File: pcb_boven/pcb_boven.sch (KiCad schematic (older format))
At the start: 28 parts

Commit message: pcb onder gemaakt
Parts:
- added BZ1: Buzzer, symbol Device:Buzzer
- added U1: miniIMU-9_v6, custom:miniIMU-9_v6, symbol miniimu-9_v6:miniIMU-9_v6
- gave numbers to parts that had none: 1
- renumbered control_board to control_board1, dip_swith_instellinen to dip_swith_instellinen1, goal_kleur to goal_kleur1
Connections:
- net labels added: A, B
- wire segments 204 -> 234
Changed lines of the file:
@@
 $EndDescr
 $Comp
-L openmv_m7_r2:openMV_M7_R2 U?
+L openmv_m7_r2:openMV_M7_R2 U2
 U 1 1 66360711
 P 9350 5325
-F 0 "U?" H 9350 6490 50  0000 C CNN
+F 0 "U2" H 9350 6490 50  0000 C CNN
 F 1 "openMV_M7_R2" H 9350 6399 50  0000 C CNN
 F 2 "custom:openmv_m7_r2" H 9350 6675 50  0001 C CNN
@@
 $EndComp
 $Comp
-L teensy:Teensy4.1 control_board
+L teensy:Teensy4.1 control_board1
 U 1 1 66362D60
 P 6125 8750
-F 0 "control_board" H 6125 11315 50  0000 C CNN
+F 0 "control_board1" H 6125 11315 50  0000 C CNN
 F 1 "Teensy4.1" H 6125 11224 50  0000 C CNN
 F 2 "" H 5725 9150 50  0001 C CNN
@@
 $EndComp
 $Comp
-L Switch:SW_DIP_x06 dip_swith_instellinen
+L Switch:SW_DIP_x06 dip_swith_instellinen1
 U 1 1 66364D70
 P 3575 7200
-F 0 "dip_swith_instellinen" H 3575 7767 50  0000 C CNN
+F 0 "dip_swith_instellinen1" H 3575 7767 50  0000 C CNN
 F 1 "SW_DIP_x06" H 3575 7676 50  0000 C CNN
 F 2 "" H 3575 7200 50  0001 C CNN
@@
 $EndComp
 $Comp
-L Switch:SW_DIP_x01 goal_kleur
+L Switch:SW_DIP_x01 goal_kleur1
 U 1 1 66365885
 P 10775 5125
-F 0 "goal_kleur" H 10775 4858 50  0000 C CNN
+F 0 "goal_kleur1" H 10775 4858 50  0000 C CNN
 F 1 "SW_DIP_x01" H 10775 4949 50  0000 C CNN
 F 2 "" H 10775 5125 50  0001 C CNN
@@
 $EndComp
 Wire Wire Line
-	7225 7300 8100 7300
+	7225 7300 7350 7300
 Wire Wire Line
 	8100 7300 8100 10775
@@
 scl
 Wire Wire Line
-	7225 7400 8075 7400
+	7225 7400 7425 7400
 Wire Wire Line
 	8075 7400 8075 10675
@@
 gnd
 Wire Wire Line
-	7225 6600 8150 6600
+	7225 6600 7675 6600
 Wire Wire Line
 	8150 6600 8150 10975
@@
 Connection ~ 4200 6025
 Wire Wire Line
-	4800 6025 7550 6025
+	4800 6025 7275 6025
 Wire Wire Line
 	7550 6025 7550 6700
@@
 	10025 4450 10025 5825
 Connection ~ 10025 5825
+$Comp
+L Device:Buzzer BZ1
+U 1 1 663737AA
+P 3950 8225
+F 0 "BZ1" H 3955 8515 50  0000 C CNN
+F 1 "Buzzer" H 3955 8424 50  0000 C CNN
+F 2 "" V 3925 8325 50  0001 C CNN
+F 3 "~" V 3925 8325 50  0001 C CNN
+	1    3950 8225
+	-1   0    0    -1
+$EndComp
+Wire Wire Line
+	4050 8125 4500 8125
+Wire Wire Line
+	4500 8125 4500 7500
+Wire Wire Line
+	4500 7500 5025 7500
+Wire Wire Line
+	2900 6025 4050 6025
+Wire Wire Line
+	4050 8325 4300 8325
+Connection ~ 4050 6025
+Wire Wire Line
+	2900 8475 4300 8475
+Wire Wire Line
+	4300 8475 4300 8325
+Wire Wire Line
+	2900 6025 2900 8475
+$Comp
+L miniimu-9_v6:miniIMU-9_v6 U1
+U 1 1 663B967A
+P 7050 4650
+F 0 "U1" H 7528 4538 50  0000 L CNN
+F 1 "miniIMU-9_v6" H 7528 4447 50  0000 L CNN
+F 2 "custom:miniIMU-9_v6" H 7050 5100 50  0001 C CNN
+F 3 "" H 7050 5100 50  0001 C CNN
+	1    7050 4650
+	1    0    0    -1
+$EndComp
+Wire Wire Line
+	7150 5250 7150 5550
+Wire Wire Line
+	7150 5550 7275 5550
+Wire Wire Line
+	7275 5550 7275 6025
+Connection ~ 7275 6025
+Wire Wire Line
+	7275 6025 7550 6025
+Wire Wire Line
+	7675 6600 7675 5500
+Wire Wire Line
+	7675 5500 7250 5500
+Wire Wire Line
+	7250 5500 7250 5250
+Connection ~ 7675 6600
+Wire Wire Line
+	7675 6600 8150 6600
+Wire Wire Line
+	7050 5250 7050 6175
+Wire Wire Line
+	7050 6175 7425 6175
+Wire Wire Line
+	7425 6175 7425 7400
+Connection ~ 7425 7400
+Wire Wire Line
+	7425 7400 8075 7400
+Wire Wire Line
+	7350 7300 7350 6250
+Wire Wire Line
+	7350 6250 6950 6250
+Wire Wire Line
+	6950 6250 6950 5250
+Connection ~ 7350 7300
+Wire Wire Line
+	7350 7300 8100 7300
+Text GLabel 1300 10175 0    50   Input ~ 0
+A
+Text GLabel 1300 10075 0    50   Input ~ 0
+B
+Wire Wire Line
+	4800 7700 5025 7700
+Wire Wire Line
+	950  10175 4800 10175
+Wire Wire Line
+	4800 10175 4800 7700
+Wire Wire Line
+	5025 7600 4775 7600
+Wire Wire Line
+	4775 7600 4775 10075
+Wire Wire Line
+	4775 10075 950  10075
 $EndSCHEMATC

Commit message: pcb onder gemaakt
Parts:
- BZ1: footprint (none) -> custom:buzer
- control_board1: footprint (none) -> custom:teensy4.1
- dip_swith_instellinen1: footprint (none) -> custom:dipswitch6
- goal_kleur1: footprint (none) -> custom:dipswitch1
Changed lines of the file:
@@
 F 0 "control_board1" H 6125 11315 50  0000 C CNN
 F 1 "Teensy4.1" H 6125 11224 50  0000 C CNN
-F 2 "" H 5725 9150 50  0001 C CNN
+F 2 "custom:teensy4.1" H 5725 9150 50  0001 C CNN
 F 3 "" H 5725 9150 50  0001 C CNN
 	1    6125 8750
@@
 F 0 "dip_swith_instellinen1" H 3575 7767 50  0000 C CNN
 F 1 "SW_DIP_x06" H 3575 7676 50  0000 C CNN
-F 2 "" H 3575 7200 50  0001 C CNN
+F 2 "custom:dipswitch6" H 3575 7200 50  0001 C CNN
 F 3 "~" H 3575 7200 50  0001 C CNN
 	1    3575 7200
@@
 F 0 "goal_kleur1" H 10775 4858 50  0000 C CNN
 F 1 "SW_DIP_x01" H 10775 4949 50  0000 C CNN
-F 2 "" H 10775 5125 50  0001 C CNN
+F 2 "custom:dipswitch1" H 10775 5125 50  0001 C CNN
 F 3 "~" H 10775 5125 50  0001 C CNN
 	1    10775 5125
@@
 F 0 "BZ1" H 3955 8515 50  0000 C CNN
 F 1 "Buzzer" H 3955 8424 50  0000 C CNN
-F 2 "" V 3925 8325 50  0001 C CNN
+F 2 "custom:buzer" V 3925 8325 50  0001 C CNN
 F 3 "~" V 3925 8325 50  0001 C CNN
 	1    3950 8225

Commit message: pcb onder gemaakt
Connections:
- wire segments 234 -> 238
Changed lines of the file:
@@
 	10025 5825 10025 6975
-Wire Wire Line
-	10025 6975 9100 6975
-Wire Wire Line
-	9100 6975 9100 10375
-Wire Wire Line
-	9100 10375 950  10375
 Wire Wire Line
 	9075 10275 9075 6800
@@
 Text GLabel 1300 10275 0    50   Input ~ 0
 3.3v
-Text GLabel 1300 10375 0    50   Input ~ 0
-gnd
 Wire Wire Line
 	11025 6800 9075 6800
@@
 Wire Wire Line
 	4775 10075 950  10075
+Wire Wire Line
+	8125 6700 8350 6700
+Wire Wire Line
+	8625 6700 8625 6975
+Wire Wire Line
+	8625 6975 10025 6975
+Connection ~ 8125 6700
+Wire Wire Line
+	8350 2350 8350 6700
+Connection ~ 8350 2350
+Connection ~ 8350 6700
+Wire Wire Line
+	8350 6700 8625 6700
+Wire Wire Line
+	8200 2375 8200 5825
+Wire Wire Line
+	8200 5825 8700 5825
+Connection ~ 8200 2375
+Connection ~ 8700 5825
 $EndSCHEMATC

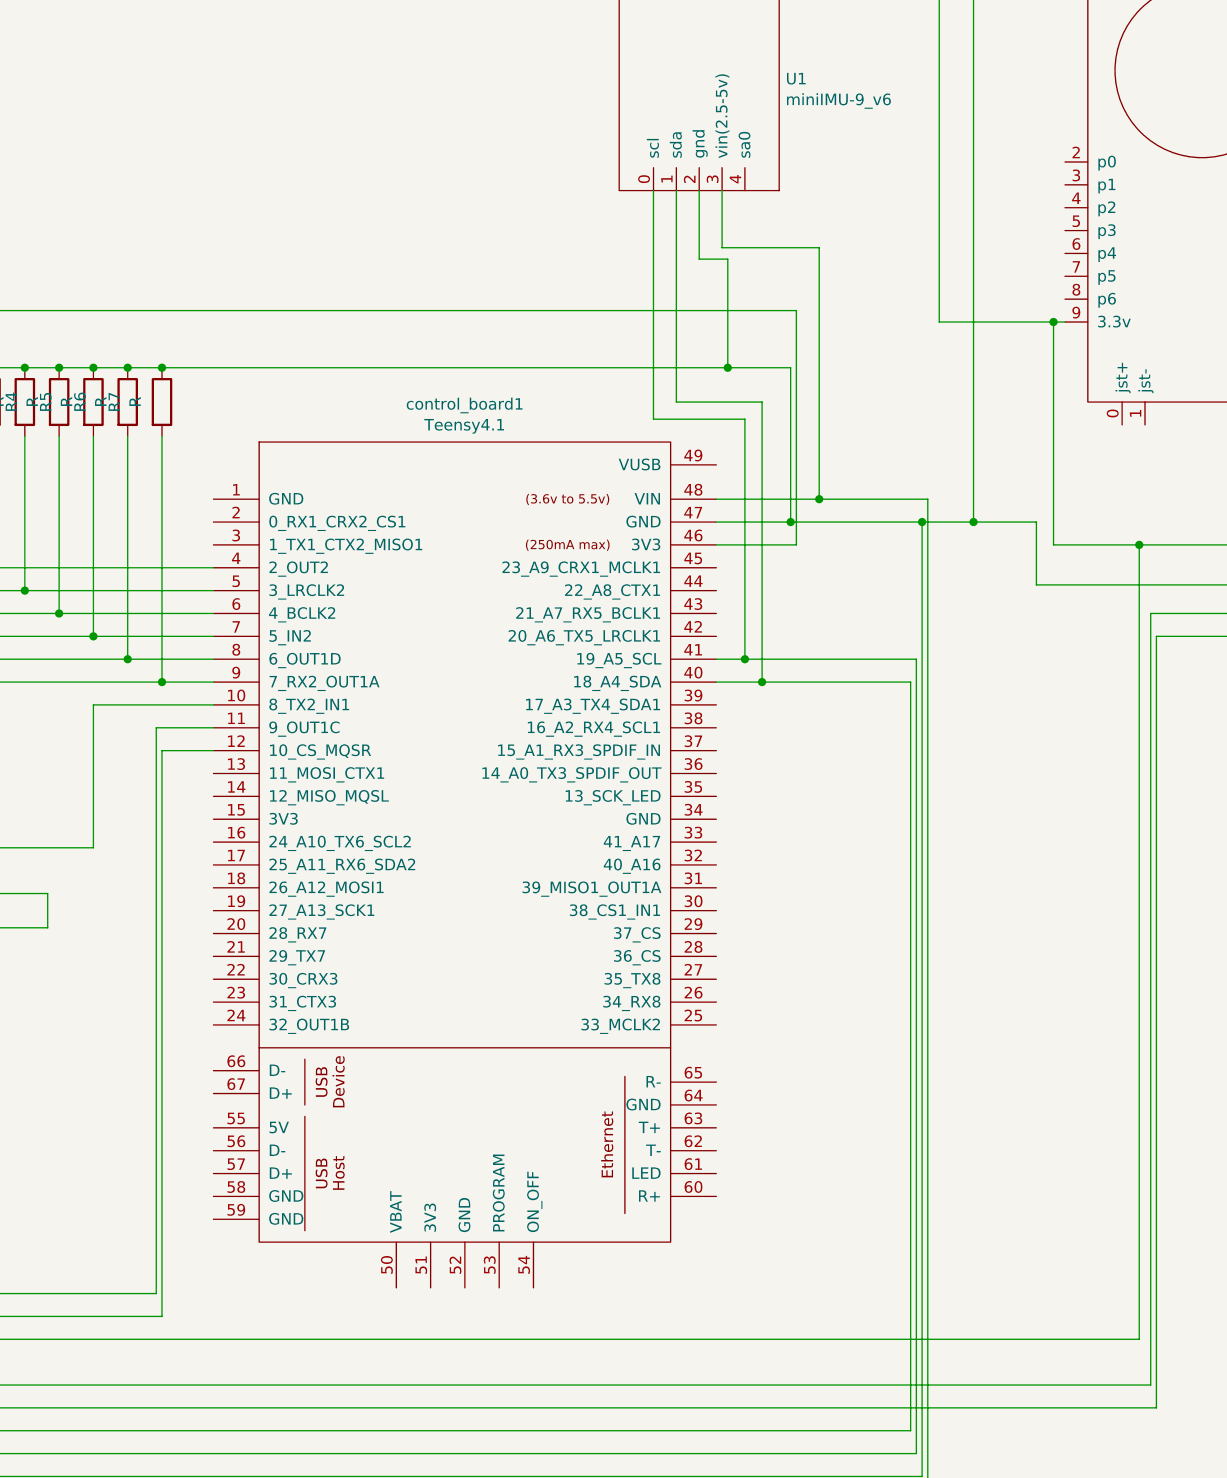
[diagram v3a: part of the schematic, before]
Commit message: add connect between teensy and openmv
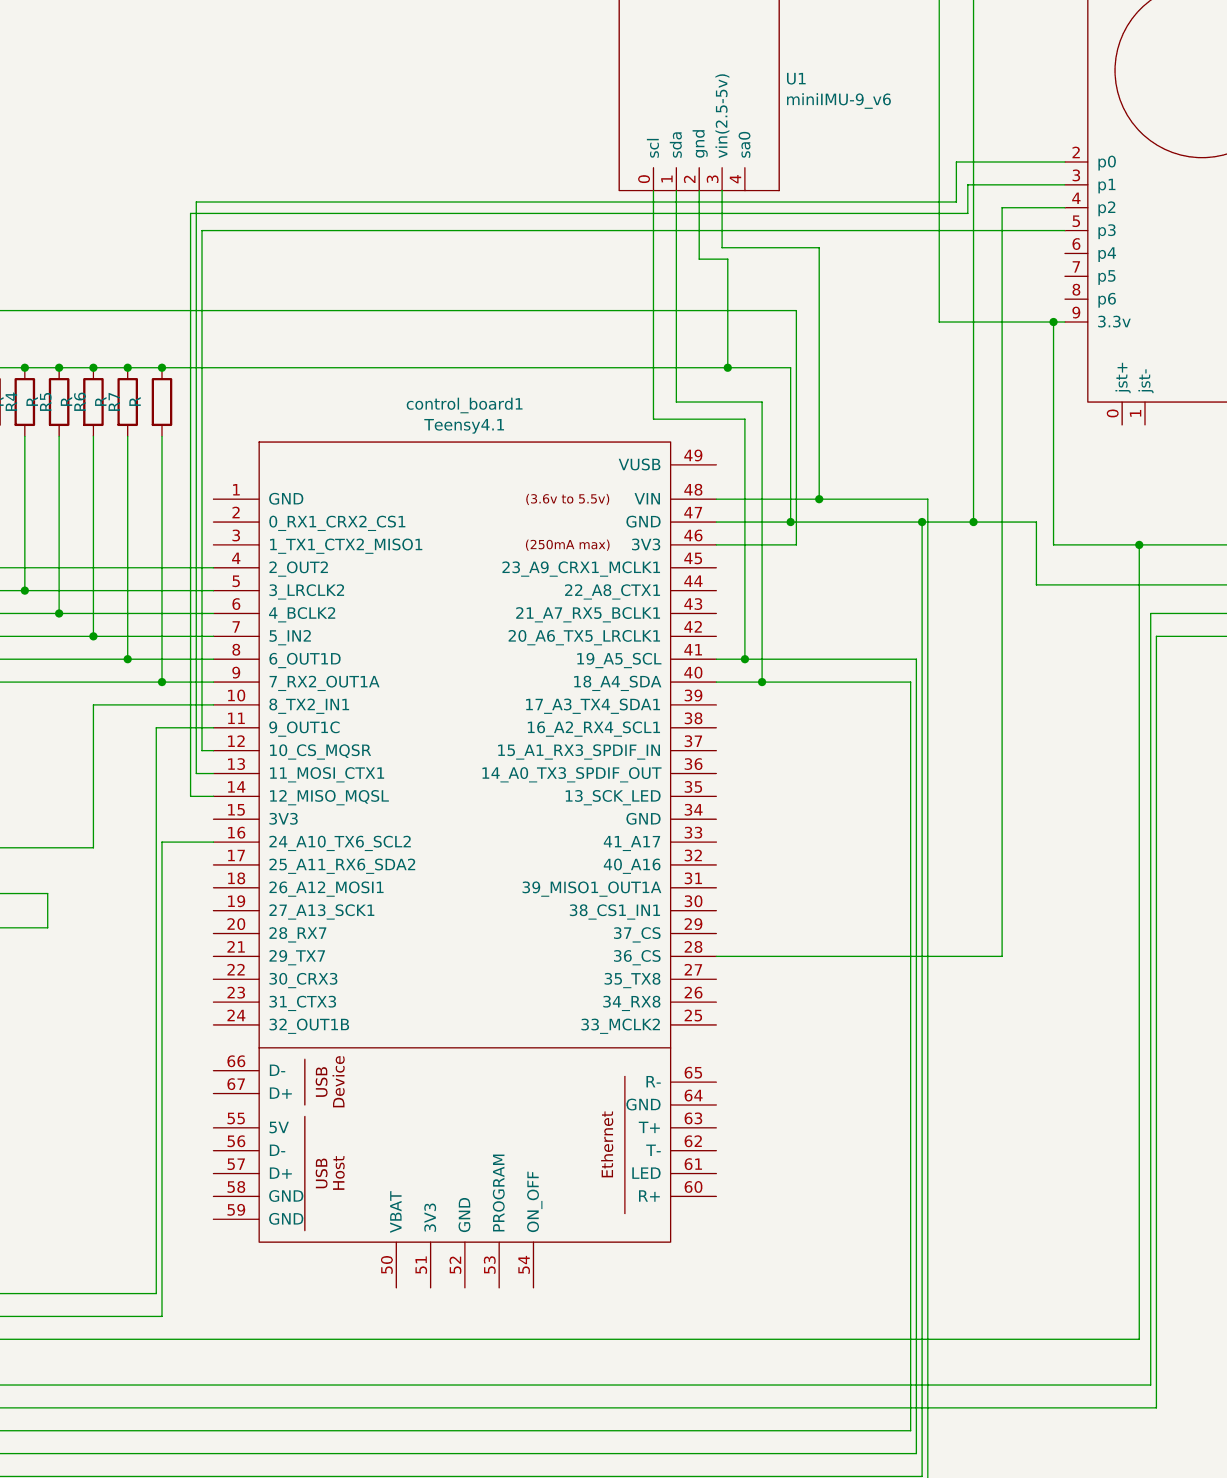
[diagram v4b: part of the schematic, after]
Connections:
- wire segments 238 -> 254
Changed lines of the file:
@@
 B
-Wire Wire Line
-	4800 7700 5025 7700
 Wire Wire Line
 	950  10175 4800 10175
 Wire Wire Line
-	4800 10175 4800 7700
+	4800 10175 4800 8100
 Wire Wire Line
 	5025 7600 4775 7600
@@
 Connection ~ 8200 2375
 Connection ~ 8700 5825
+Wire Wire Line
+	8750 5425 4975 5425
+Wire Wire Line
+	4975 5425 4975 7700
+Wire Wire Line
+	4975 7700 5025 7700
+Wire Wire Line
+	5025 8100 4800 8100
+Wire Wire Line
+	5025 7800 4950 7800
+Wire Wire Line
+	4950 7800 4950 5300
+Wire Wire Line
+	4950 5300 8275 5300
+Wire Wire Line
+	8275 5300 8275 5125
+Wire Wire Line
+	8275 5125 8750 5125
+Wire Wire Line
+	8750 5225 8325 5225
+Wire Wire Line
+	8325 5225 8325 5350
+Wire Wire Line
+	8325 5350 4925 5350
+Wire Wire Line
+	4925 5350 4925 7900
+Wire Wire Line
+	4925 7900 5025 7900
+Wire Wire Line
+	7225 8600 8475 8600
+Wire Wire Line
+	8475 8600 8475 5325
+Wire Wire Line
+	8475 5325 8750 5325
 $EndSCHEMATC

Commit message: add mcp
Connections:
- wire segments 254 -> 268
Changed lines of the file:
@@
 Connection ~ 7425 7400
-Wire Wire Line
-	7425 7400 8075 7400
 Wire Wire Line
 	7350 7300 7350 6250
@@
 	6950 6250 6950 5250
 Connection ~ 7350 7300
-Wire Wire Line
-	7350 7300 8100 7300
 Text GLabel 1300 10175 0    50   Input ~ 0
 A
@@
 Wire Wire Line
 	8125 6700 8350 6700
-Wire Wire Line
-	8625 6700 8625 6975
 Wire Wire Line
 	8625 6975 10025 6975
@@
 Wire Wire Line
 	8475 5325 8750 5325
+Wire Wire Line
+	7350 7300 8100 7300
+Wire Wire Line
+	8625 5525 8625 6700
+Connection ~ 8625 6700
+Wire Wire Line
+	8625 6700 8625 6975
+Connection ~ 8625 6975
+Wire Wire Line
+	8625 6975 8625 7300
+Connection ~ 8100 7300
+Wire Wire Line
+	8100 7300 8625 7300
+Wire Wire Line
+	8650 5625 8650 7400
+Wire Wire Line
+	7425 7400 8075 7400
+Connection ~ 8075 7400
+Wire Wire Line
+	8075 7400 8650 7400
+Wire Wire Line
+	8750 5525 8625 5525
+Wire Wire Line
+	8625 5525 5000 5525
+Wire Wire Line
+	5000 5525 5000 6700
+Wire Wire Line
+	5000 6700 5025 6700
+Connection ~ 8625 5525
+Wire Wire Line
+	5025 6800 5025 6750
+Wire Wire Line
+	5025 6750 5050 6750
+Wire Wire Line
+	5050 6750 5050 5625
+Wire Wire Line
+	5050 5625 8650 5625
+Connection ~ 8650 5625
+Wire Wire Line
+	8650 5625 8750 5625
 $EndSCHEMATC

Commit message: pcb
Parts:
- added 3V3_converter1: CC6-1203SR-E, custom:CC60512SRE, symbol cc6-1203sr-e:CC6-1203SR-E
- added 5V_converter1: SFTN01M-05N, custom:SFTN01M05N, symbol sftn01m-05n:SFTN01M-05N
- added xt30: Battery, Connector_AMASS:AMASS_XT30U-F_1x02_P5.0mm_Vertical, symbol Device:Battery
- added xt60: Battery, Connector_AMASS:AMASS_XT60-F_1x02_P7.20mm_Vertical, symbol Device:Battery
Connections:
- wire segments 268 -> 294
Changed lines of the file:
@@
 	9950 5825 10025 5825
-Wire Wire Line
-	10025 5825 10025 6975
 Wire Wire Line
 	9075 10275 9075 6800
@@
 Wire Wire Line
 	8700 5825 8700 6800
-Wire Wire Line
-	11025 9000 10025 9000
-Wire Wire Line
-	10025 9000 10025 6975
-Connection ~ 10025 6975
 Wire Wire Line
 	825  2275 825  2350
@@
 Wire Wire Line
 	10025 4450 10025 5825
-Connection ~ 10025 5825
 $Comp
 L Device:Buzzer BZ1
@@
 	4500 7500 5025 7500
 Wire Wire Line
-	2900 6025 4050 6025
-Wire Wire Line
 	4050 8325 4300 8325
 Connection ~ 4050 6025
@@
 Wire Wire Line
 	8125 6700 8350 6700
-Wire Wire Line
-	8625 6975 10025 6975
 Connection ~ 8125 6700
 Wire Wire Line
 	8350 2350 8350 6700
 Connection ~ 8350 2350
-Connection ~ 8350 6700
-Wire Wire Line
-	8350 6700 8625 6700
-Wire Wire Line
-	8200 2375 8200 5825
+Wire Wire Line
+	8200 2375 8200 3875
 Wire Wire Line
 	8200 5825 8700 5825
@@
 Wire Wire Line
 	7350 7300 8100 7300
-Wire Wire Line
-	8625 5525 8625 6700
-Connection ~ 8625 6700
-Wire Wire Line
-	8625 6700 8625 6975
-Connection ~ 8625 6975
-Wire Wire Line
-	8625 6975 8625 7300
 Connection ~ 8100 7300
 Wire Wire Line
@@
 Wire Wire Line
 	8650 5625 8750 5625
+$Comp
+L Device:Battery xt60
+U 1 1 6666BA64
+P 1975 5125
+F 0 "xt60" H 2083 5171 50  0000 L CNN
+F 1 "Battery" H 2083 5080 50  0000 L CNN
+F 2 "Connector_AMASS:AMASS_XT60-F_1x02_P7.20mm_Vertical" V 1975 5185 50  0001 C CNN
+F 3 "https://eu.mouser.com/datasheet/2/813/xt60-2490175.pdf" V 1975 5185 50  0001 C CNN
+	1    1975 5125
+	1    0    0    -1
+$EndComp
+$Comp
+L Device:Battery xt30
+U 1 1 6666CC1A
+P 1600 5125
+F 0 "xt30" H 1708 5171 50  0000 L CNN
+F 1 "Battery" H 1708 5080 50  0000 L CNN
+F 2 "Connector_AMASS:AMASS_XT30U-F_1x02_P5.0mm_Vertical" V 1600 5185 50  0001 C CNN
+F 3 "https://eu.mouser.com/ProductDetail/DFRobot/FIT0586?qs=w%2Fv1CP2dgqouWR8IxqIK1w%3D%3D" V 1600 5185 50  0001 C CNN
+	1    1600 5125
+	1    0    0    -1
+$EndComp
+$Comp
+L cc6-1203sr-e:CC6-1203SR-E 3V3_converter1
+U 1 1 66680960
+P 2600 4300
+F 0 "3V3_converter1" H 3300 4565 50  0000 C CNN
+F 1 "CC6-1203SR-E" H 3300 4474 50  0000 C CNN
+F 2 "custom:CC60512SRE" H 3850 4400 50  0001 L CNN
+F 3 "https://product.tdk.com/system/files/dam/doc/product/power/switching-power/dc-dc-converter/catalog/cc-e_e.pdf" H 3850 4300 50  0001 L CNN
+F 4 "DC-DC Converters, On-board type, Output: 3.96W, 3.3V, Isolated type, Option: SMD type" H 3850 4200 50  0001 L CNN "Description"
+F 5 "8.8" H 3850 4100 50  0001 L CNN "Height"
+F 6 "TDK" H 3850 4000 50  0001 L CNN "Manufacturer_Name"
+F 7 "CC6-1203SR-E" H 3850 3900 50  0001 L CNN "Manufacturer_Part_Number"
+F 8 "967-CC6-1203SR-E" H 3850 3800 50  0001 L CNN "Mouser Part Number"
+F 9 "https://www.mouser.co.uk/ProductDetail/TDK-Lambda/CC6-1203SR-E?qs=Vwh6e7toGLi4J%2FzloL2n3g%3D%3D" H 3850 3700 50  0001 L CNN "Mouser Price/Stock"
+F 10 "CC6-1203SR-E" H 3850 3600 50  0001 L CNN "Arrow Part Number"
+F 11 "https://www.arrow.com/en/products/cc6-1203sr-e/tdk-lambda-americas?region=nac" H 3850 3500 50  0001 L CNN "Arrow Price/Stock"
+	1    2600 4300
+	1    0    0    -1
+$EndComp
+$Comp
+L sftn01m-05n:SFTN01M-05N 5V_converter1
+U 1 1 66681E5D
+P 2625 4825
+F 0 "5V_converter1" H 3275 5090 50  0000 C CNN
+F 1 "SFTN01M-05N" H 3275 4999 50  0000 C CNN
+F 2 "custom:SFTN01M05N" H 3775 4925 50  0001 L CNN
+F 3 "https://www.meanwell.com/webapp/product/search.aspx?prod=SFTN01-N" H 3775 4825 50  0001 L CNN
+F 4 "Isolated DC/DC Converters - SMD 1W 12Vin 5Vout 20-200mA SMT Unregulated" H 3775 4725 50  0001 L CNN "Description"
+F 5 "7.6" H 3775 4625 50  0001 L CNN "Height"
+F 6 "Mean Well" H 3775 4525 50  0001 L CNN "Manufacturer_Name"
+F 7 "SFTN01M-05N" H 3775 4425 50  0001 L CNN "Manufacturer_Part_Number"
+F 8 "709-SFTN01M-05N" H 3775 4325 50  0001 L CNN "Mouser Part Number"
+F 9 "https://www.mouser.co.uk/ProductDetail/MEAN-WELL/SFTN01M-05N?qs=A6eO%252BMLsxmQLvWwJN5Fn%252BQ%3D%3D" H 3775 4225 50  0001 L CNN "Mouser Price/Stock"
+	1    2625 4825
+	1    0    0    -1
+$EndComp
+Wire Wire Line
+	1600 4925 1975 4925
+Wire Wire Line
+	1975 5325 1600 5325
+Wire Wire Line
+	1975 5325 2300 5325
+Wire Wire Line
+	2300 5325 2300 4825
+Wire Wire Line
+	2300 4825 2625 4825
+Connection ~ 1975 5325
+Wire Wire Line
+	1975 4925 2625 4925
+Connection ~ 1975 4925
+Wire Wire Line
+	2300 4825 2300 4500
+Wire Wire Line
+	2300 4500 2600 4500
+Connection ~ 2300 4825
+Wire Wire Line
+	1975 4925 1975 4300
+Wire Wire Line
+	1975 4300 2600 4300
+Wire Wire Line
+	4000 4300 4550 4300
+Wire Wire Line
+	4550 4300 4550 3875
+Wire Wire Line
+	4550 3875 8200 3875
+Connection ~ 8200 3875
+Wire Wire Line
+	8200 3875 8200 5825
+Connection ~ 10025 5825
+Wire Wire Line
+	8625 5525 8625 7300
+Wire Wire Line
+	10025 5825 10025 6700
+Wire Wire Line
+	8350 6700 10025 6700
+Connection ~ 8350 6700
+Connection ~ 10025 6700
+Wire Wire Line
+	10025 6700 10025 9000
+Wire Wire Line
+	7250 5500 4225 5500
+Wire Wire Line
+	4225 5500 4225 5125
+Wire Wire Line
+	4225 5125 3925 5125
+Connection ~ 7250 5500
+Wire Wire Line
+	2625 5125 2525 5125
+Wire Wire Line
+	2525 5125 2525 5625
+Wire Wire Line
+	2525 5625 3750 5625
+Wire Wire Line
+	4125 5625 4125 4500
+Wire Wire Line
+	4125 4500 4000 4500
+Wire Wire Line
+	3750 5625 3750 6025
+Wire Wire Line
+	2900 6025 3750 6025
+Connection ~ 3750 5625
+Wire Wire Line
+	3750 5625 4125 5625
+Connection ~ 3750 6025
+Wire Wire Line
+	3750 6025 4050 6025
+Wire Wire Line
+	10325 8700 10325 8600
+Wire Wire Line
+	10325 8600 10325 8500
+Connection ~ 10325 8600
+Wire Wire Line
+	10325 8700 10325 9000
+Wire Wire Line
+	10025 9000 10325 9000
+Connection ~ 10325 8700
+Connection ~ 10325 9000
+Wire Wire Line
+	10325 9000 11025 9000
 $EndSCHEMATC
